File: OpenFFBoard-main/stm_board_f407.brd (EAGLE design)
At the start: 60 x 60 mm, 59 parts, among them J1 10118193-0001LF, SW1 TL3342F160QG/TR, SW2 TL3342F160QG/TR, U1 STM32F407VGT6, U2 TJA1051T/3, U3 LM1117, X1 8MHz

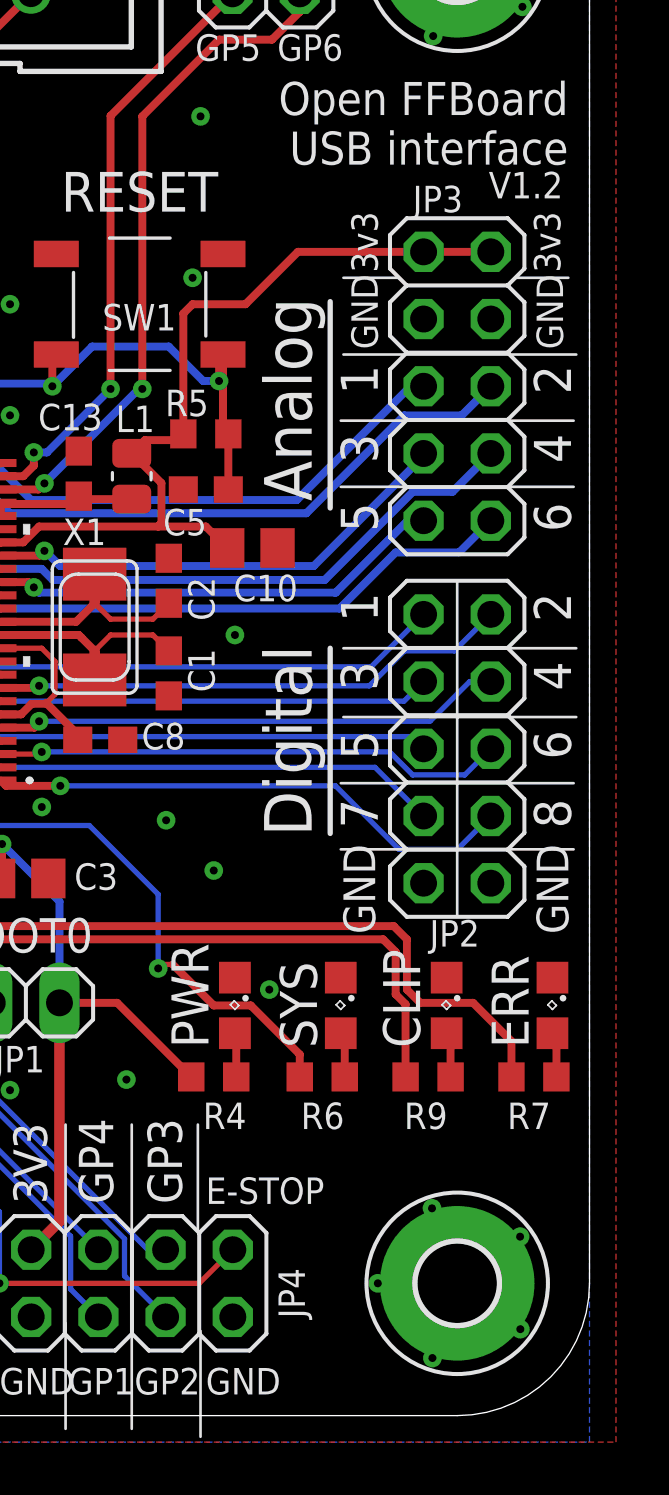
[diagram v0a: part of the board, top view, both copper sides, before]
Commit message: Added E-Stop cap
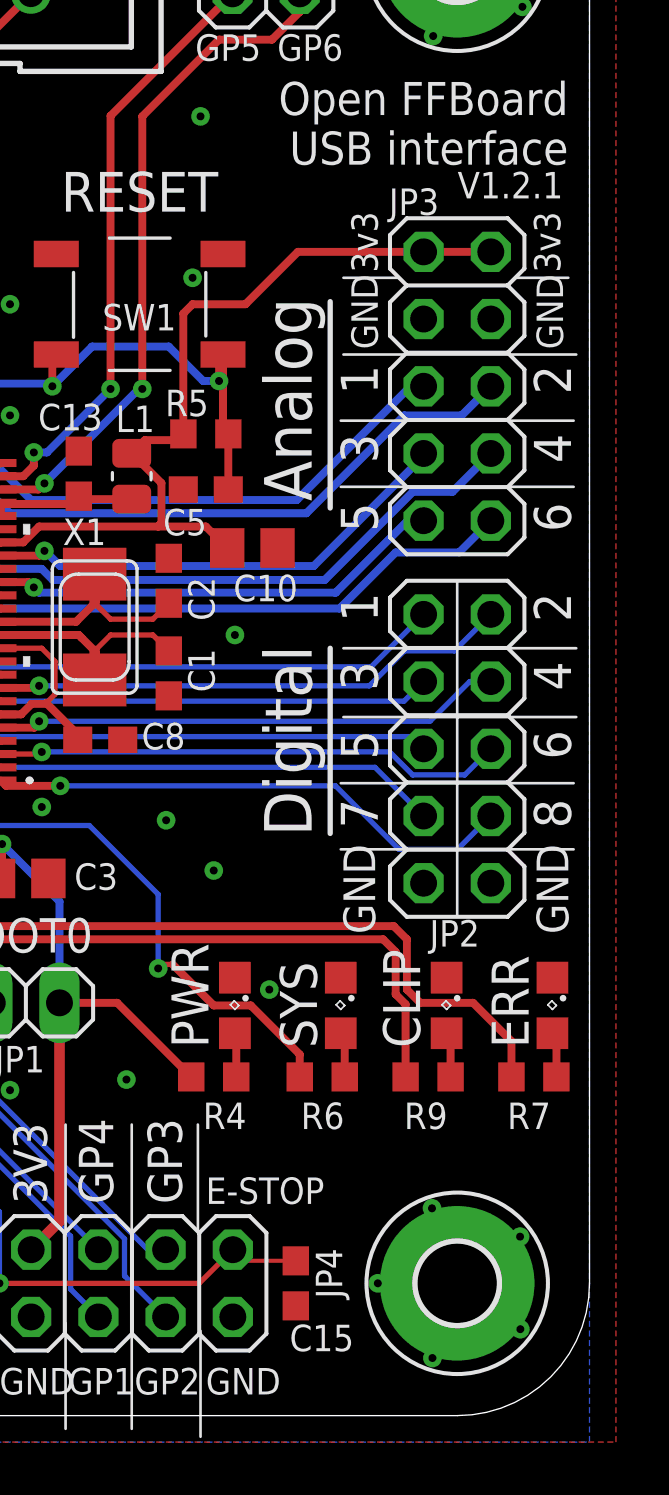
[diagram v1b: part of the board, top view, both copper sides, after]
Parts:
- added C15: 100nF, resistor:C0603
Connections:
- net E_STOP: now also C15.1
- net GND: now also C15.2
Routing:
- net E_STOP: track 30.2 -> 32.8 mm
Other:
- board text added: "V1.2.1"
- board text removed: "V1.2"
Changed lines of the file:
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@@
 <text x="59.2" y="-9.6" size="1.25" layer="21" rot="R180">Open FFBoard
 USB interface</text>
-<text x="59" y="-13" size="1" layer="21" rot="R180">V1.2</text>
+<text x="59" y="-13" size="1" layer="21" rot="R180">V1.2.1</text>
 <text x="21.5" y="-8.55" size="1" layer="22" font="vector" rot="MR270">GND | 5V</text>
 <text x="24" y="-8.5" size="1" layer="22" font="vector" rot="MR270">RST | 3V3</text>
@@
 <text x="47.4" y="-1.3" size="0.8128" layer="22" font="vector" rot="MR0">TX</text>
 <text x="49.9" y="-9.5" size="0.8128" layer="22" font="vector" rot="MR0">TIM/ADC</text>
-<text x="47.6" y="-13.3" size="1" layer="22" font="vector" rot="MR180">V1.2</text>
+<text x="47.6" y="-13.3" size="1" layer="22" font="vector" rot="MR180">V1.2.1</text>
 <wire x1="3" y1="-26.7" x2="7.8" y2="-26.7" width="0.1016" layer="21"/>
 <wire x1="4.2" y1="-26.7" x2="2.9" y2="-26.7" width="0.1" layer="22"/>
@@
 </element>
 <element name="JP3" library="pinhead" library_urn="urn:adsk.eagle:library:325" package="2X05" package3d_urn="urn:adsk.eagle:package:22470/2" value="Analog" x="55" y="-21.1" locked="yes" smashed="yes" rot="R270">
-<attribute name="NAME" x="53.32" y="-14.525" size="1" layer="25" ratio="10"/>
+<attribute name="NAME" x="52.42" y="-14.625" size="1" layer="25" ratio="10"/>
 <attribute name="POPULARITY" value="35" x="55" y="-21.1" size="1.778" layer="27" rot="R270" display="off"/>
 <attribute name="VALUE" x="50.555" y="-16.02" size="1.27" layer="27" rot="R270"/>
@@
 </element>
 <element name="JP4" library="pinhead" library_urn="urn:adsk.eagle:library:325" package="2X11" package3d_urn="urn:adsk.eagle:package:22419/2" value="EXT" x="33.82" y="-55" locked="yes" smashed="yes" rot="R180">
-<attribute name="NAME" x="49.245" y="-56.32" size="1" layer="25" ratio="10" rot="R90"/>
+<attribute name="NAME" x="49.655" y="-53.68" size="1" layer="25" ratio="10" rot="R270"/>
 <attribute name="POPULARITY" value="2" x="33.82" y="-55" size="1.778" layer="27" rot="R180" display="off"/>
 <attribute name="VALUE" x="41.44" y="-50.555" size="1.27" layer="27" rot="R180"/>
@@
 <attribute name="POPULARITY" value="69" x="17.6" y="-47.6" size="1.778" layer="27" display="off"/>
 <attribute name="VALUE" x="11.25" y="-50.775" size="1.27" layer="27"/>
+</element>
+<element name="C15" library="resistor" library_urn="urn:adsk.eagle:library:348" package="C0603" package3d_urn="urn:adsk.eagle:package:23616/2" value="100nF" x="48.9" y="-55" locked="yes" smashed="yes" rot="R270">
+<attribute name="NAME" x="48.665" y="-57.565" size="1" layer="25"/>
+<attribute name="VALUE" x="46.995" y="-54.365" size="1.27" layer="27" rot="R270"/>
 </element>
 </elements>
@@
 <via x="15.8" y="-41.9" extent="1-16" drill="0.3"/>
 <via x="13.5" y="-44.2" extent="1-16" drill="0.3"/>
+<contactref element="C15" pad="2"/>
 </signal>
 <signal name="+3V3">
@@
 <wire x1="37.7" y1="-55" x2="45.25" y2="-55" width="0.2" layer="1"/>
 <wire x1="45.25" y1="-55" x2="46.52" y2="-53.73" width="0.2" layer="1"/>
+<contactref element="C15" pad="1"/>
+<wire x1="46.52" y1="-53.73" x2="46.94" y2="-54.15" width="0.1524" layer="1"/>
+<wire x1="46.94" y1="-54.15" x2="48.9" y2="-54.15" width="0.1524" layer="1"/>
 </signal>
 </signals>
